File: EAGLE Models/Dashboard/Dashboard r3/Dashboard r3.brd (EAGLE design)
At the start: 105.5 x 67.2 mm, 73 parts, among them IC1 AT90CAN128, IC2 MCP2551SO8, IC3 NUP2105L, Q1 56P2859, U1 74LCX125M

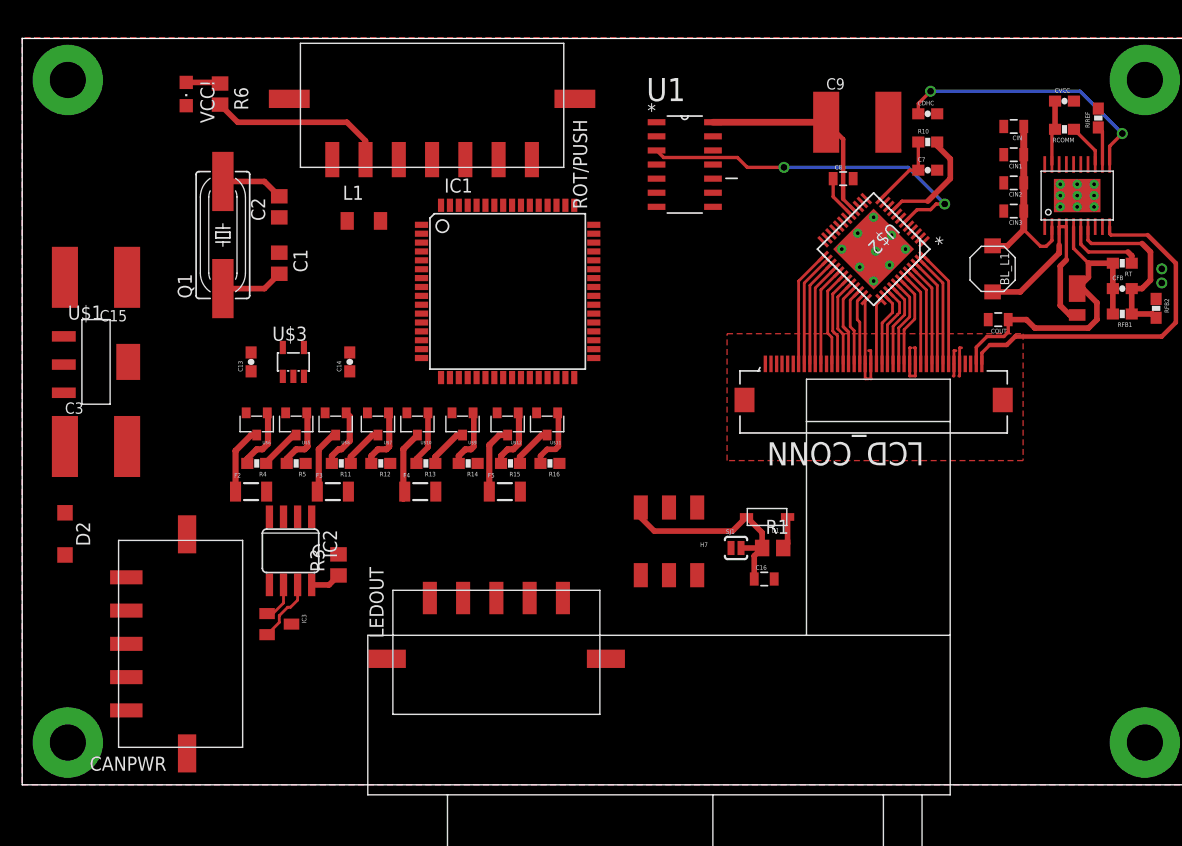
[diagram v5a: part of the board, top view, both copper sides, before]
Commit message: Finished routing traces and began fixing drc errors
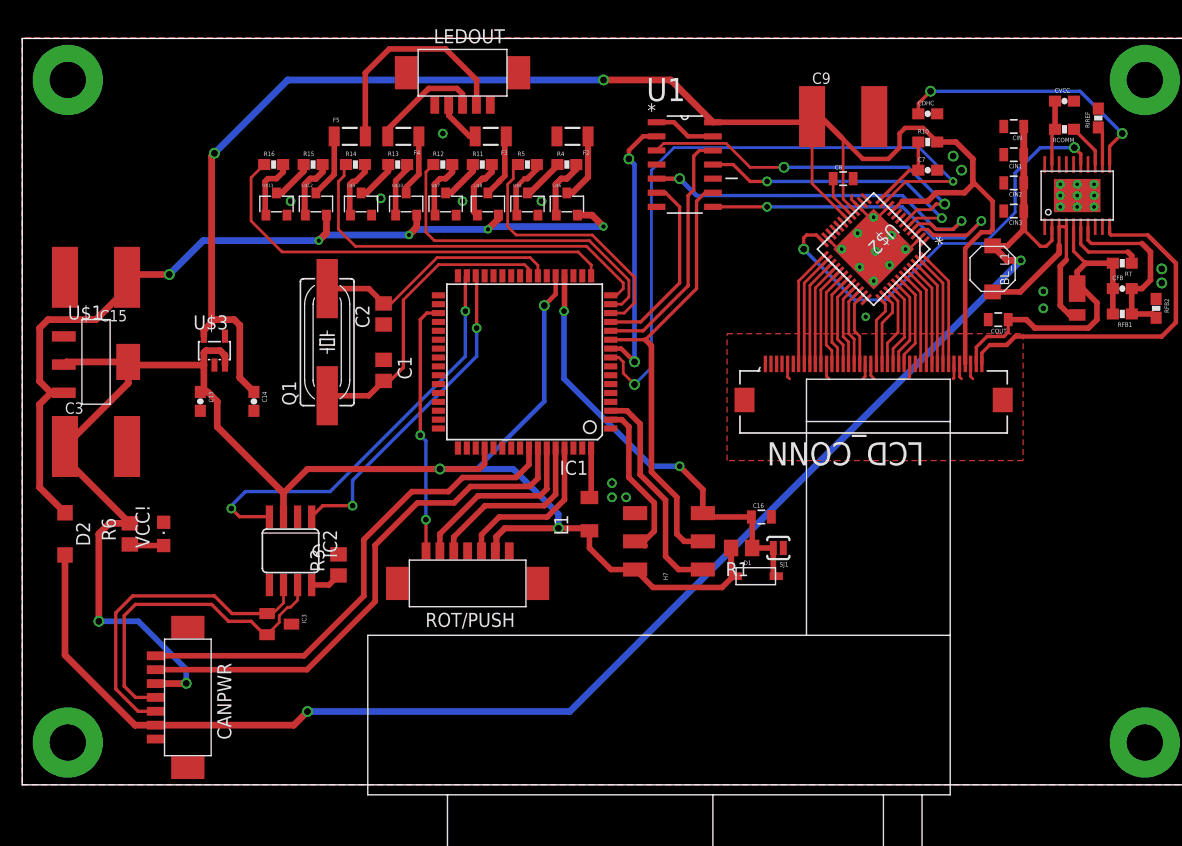
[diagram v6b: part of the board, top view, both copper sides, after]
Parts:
- CANPWR: device molex:43650-0513 -> molex:53261-0771
- LEDOUT: device molex:43650-0513 -> molex:53261-0571
- ROT/PUSH: device molex:43650-0513-7 -> molex:53261-0771
- moved F2 43.2 mm to (48.0, 58.4), turned to 180 degrees
- moved LEDOUT 42.3 mm to (38.1, 60.5), turned to 180 degrees
- moved R6 40.4 mm to (8.13, 22.6), turned to 90 degrees
- moved VCC! 39.7 mm to (11.2, 22.6), turned to 0 degrees
- moved R4 38.8 mm to (47.5, 55.9), turned to 0 degrees
- moved R16 36.7 mm to (21.1, 55.9), turned to 0 degrees
- moved F3 35.0 mm to (40.6, 58.4), turned to 180 degrees
- moved F5 34.9 mm to (27.9, 58.4)
- moved U$6 34.3 mm to (47.5, 52.3), turned to 0 degrees
- moved R5 34.0 mm to (43.9, 55.9), turned to 0 degrees
- moved L1 33.3 mm to (49.5, 24.4), turned to 90 degrees
- moved ROT/PUSH 33.2 mm to (38.6, 21.8), turned to 0 degrees
- moved R15 32.3 mm to (24.6, 55.9), turned to 0 degrees
- moved F4 32.0 mm to (32.8, 58.4), turned to 180 degrees
- moved U$11 31.4 mm to (21.3, 52.3), turned to 0 degrees
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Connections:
- removed net TCK: IC1.57
- new net PF4: CANPWR.7, IC1.57
- net GND: now also LEDOUT.5, LEDOUT.GND1, LEDOUT.GND2, ROT/PUSH.7, ROT/PUSH.GND1, ROT/PUSH.GND2
- net PF3: now also CANPWR.6
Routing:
- net VCC: track 19.1 -> 165.6 mm, vias 0 -> 5
- net 3.3V: track 29.4 -> 150.2 mm, vias 0 -> 2
- net 12V: track 17.3 -> 135.5 mm, vias 0 -> 2
- net 12V_PROTECTED: track 0.00 -> 83.9 mm, vias 0 -> 5
- net INT_N: track 0.00 -> 59.9 mm, vias 0 -> 2
- net PF3: track 0.00 -> 47.3 mm
- net PF4: track 0.00 -> 45.2 mm
- net AVR_SCLK: track 0.00 -> 40.6 mm
- net BACKLIGHT_CTRL: track 0.00 -> 38.9 mm, vias 0 -> 2
- net PB7(PWM): track 0.00 -> 38.8 mm
- net RXCAN: track 0.00 -> 38.0 mm, vias 0 -> 2
- net PB6(PWM): track 0.00 -> 35.7 mm
- net FT801_MISO: track 0.00 -> 34.9 mm, vias 0 -> 2
- net FT801_SCLK: track 0.00 -> 32.7 mm, vias 0 -> 2
- net PB5(PWM): track 0.00 -> 29.9 mm
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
